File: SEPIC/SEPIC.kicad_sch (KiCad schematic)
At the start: 17 parts, among them J1 Screw Terminal, J2 Barrel Jack, J3 Pin Header, J4 Screw Terminal, Q1 IRF520N, U1 HCPL-3120

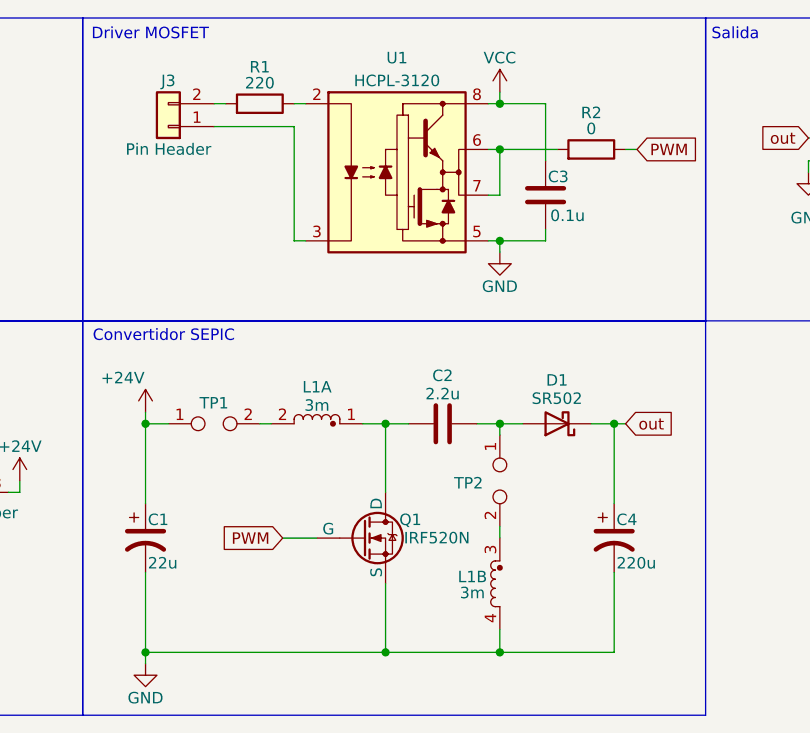
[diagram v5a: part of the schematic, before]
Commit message: Agregar puntos medición corriente
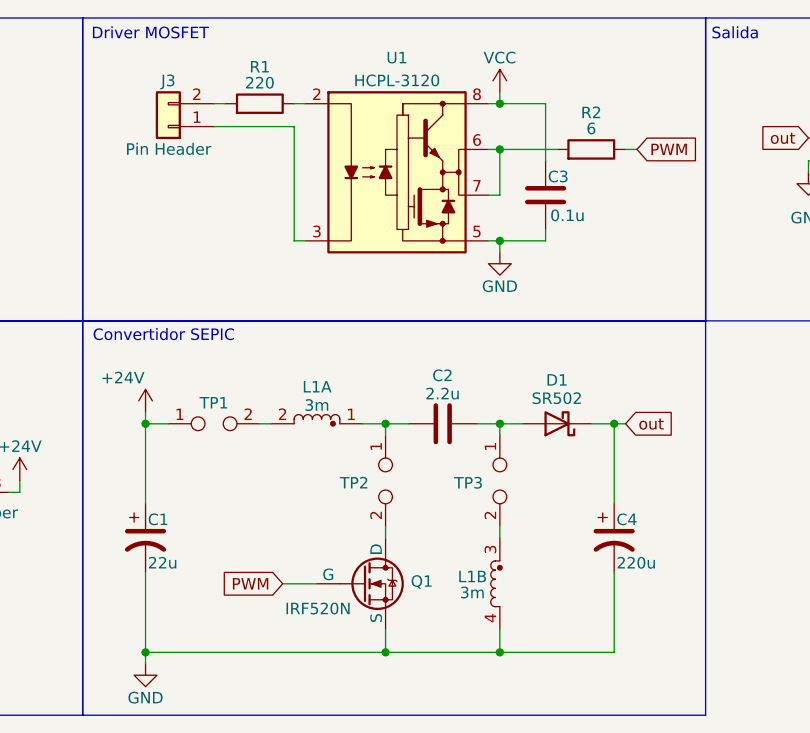
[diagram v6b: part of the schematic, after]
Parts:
- added TP2: Shunt, Resistor_THT:R_Axial_DIN0411_L9.9mm_D3.6mm_P12.70mm_Horizontal, symbol Connector:TestPoint_2Pole
- R2: value 0 -> 6
- TP1: footprint TestPoint:TestPoint_2Pads_Pitch5.08mm_Drill1.3mm -> Resistor_THT:R_Axial_DIN0411_L9.9mm_D3.6mm_P12.70mm_Horizontal
- TP3: renamed from TP2; footprint TestPoint:TestPoint_2Pads_Pitch5.08mm_Drill1.3mm -> Resistor_THT:R_Axial_DIN0411_L9.9mm_D3.6mm_P12.70mm_Horizontal
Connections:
- net at C2.1, L1.1: now also TP2.1; no longer Q1.2 (D)
- new net: Q1.2 (D), TP2.2
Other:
- moved on the sheet: Q1
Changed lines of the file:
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@@
 	(wire
 		(pts
-			(xy 88.9 80.01) (xy 92.71 80.01)
+			(xy 88.9 85.09) (xy 92.71 85.09)
 		)
 		(stroke
@@
 	(wire
 		(pts
-			(xy 100.33 67.31) (xy 100.33 74.93)
-		)
-		(stroke
-			(width 0)
-			(type default)
-		)
-	)
-	(wire
-		(pts
-			(xy 100.33 85.09) (xy 100.33 92.71)
+			(xy 100.33 67.31) (xy 100.33 68.58)
 		)
 		(stroke
@@
 	(wire
 		(pts
+			(xy 100.33 90.17) (xy 100.33 92.71)
+		)
+		(stroke
+			(width 0)
+			(type default)
+		)
+	)
+	(wire
+		(pts
 			(xy 113.03 46.99) (xy 113.03 48.26)
 		)
@@
 		(pts
 			(xy 123.19 67.31) (xy 125.73 67.31)
+		)
+		(stroke
+			(width 0)
+			(type default)
+		)
+	)
+	(wire
+		(pts
+			(xy 100.33 78.74) (xy 100.33 80.01)
 		)
 		(stroke
@@
 	(global_label "PWM"
 		(shape input)
-		(at 88.9 80.01 180)
+		(at 88.9 85.09 180)
 		(fields_autoplaced yes)
 		(effects
@@
 		)
 		(property "Intersheetrefs" "${INTERSHEET_REFS}"
-			(at 81.742 80.01 0)
+			(at 81.742 85.09 0)
 			(effects
 				(font
@@
 		(on_board yes)
 		(dnp no)
-		(property "Reference" "TP2"
+		(property "Reference" "TP3"
 			(at 107.95 73.914 90)
 			(effects
@@
 			)
 		)
-		(property "Footprint" "TestPoint:TestPoint_2Pads_Pitch5.08mm_Drill1.3mm"
+		(property "Footprint" "Resistor_THT:R_Axial_DIN0411_L9.9mm_D3.6mm_P12.70mm_Horizontal"
 			(at 113.03 73.66 0)
 			(effects
@@
 			(project ""
 				(path "/cb0f21c9-e6cc-49b2-a40a-07d77f15ad11"
-					(reference "TP2")
+					(reference "TP3")
 					(unit 1)
 				)
@@
 			)
 		)
-		(property "Value" "0"
+		(property "Value" "6"
 			(at 123.19 34.544 90)
 			(effects
@@
 	)
 	(symbol
+		(lib_id "Connector:TestPoint_2Pole")
+		(at 100.33 73.66 270)
+		(unit 1)
+		(exclude_from_sim no)
+		(in_bom yes)
+		(on_board yes)
+		(dnp no)
+		(property "Reference" "TP2"
+			(at 95.25 73.914 90)
+			(effects
+				(font
+					(size 1.27 1.27)
+				)
+				(justify left)
+			)
+		)
+		(property "Value" "Shunt"
+			(at 99.06 74.93 0)
+			(effects
+				(font
+					(size 1.27 1.27)
+				)
+				(justify left)
+				(hide yes)
+			)
+		)
+		(property "Footprint" "Resistor_THT:R_Axial_DIN0411_L9.9mm_D3.6mm_P12.70mm_Horizontal"
+			(at 100.33 73.66 0)
+			(effects
+				(font
+					(size 1.27 1.27)
+				)
+				(hide yes)
+			)
+		)
+		(property "Datasheet" "~"
+			(at 100.33 73.66 0)
+			(effects
+				(font
+					(size 1.27 1.27)
+				)
+				(hide yes)
+			)
+		)
+		(property "Description" "2-polar test point"
+			(at 100.33 73.66 0)
+			(effects
+				(font
+					(size 1.27 1.27)
+				)
+				(hide yes)
+			)
+		)
+		(pin "2"
+		)
+		(pin "1"
+		)
+		(instances
+			(project "SEPIC"
+				(path "/cb0f21c9-e6cc-49b2-a40a-07d77f15ad11"
+					(reference "TP2")
+					(unit 1)
+				)
+			)
+		)
+	)
+	(symbol
 		(lib_id "power:VCC")
 		(at 113.03 30.48 0)
@@
 			)
 		)
-		(property "Footprint" "TestPoint:TestPoint_2Pads_Pitch5.08mm_Drill1.3mm"
+		(property "Footprint" "Resistor_THT:R_Axial_DIN0411_L9.9mm_D3.6mm_P12.70mm_Horizontal"
 			(at 81.28 67.31 0)
 			(effects
@@
 	(symbol
 		(lib_id "Simulation_SPICE:NMOS")
-		(at 97.79 80.01 0)
+		(at 97.79 85.09 0)
 		(unit 1)
 		(exclude_from_sim no)
@@
 		(dnp no)
 		(property "Reference" "Q1"
-			(at 101.854 77.978 0)
+			(at 103.124 84.836 0)
 			(effects
 				(font
@@
 		)
 		(property "Value" "IRF520N"
-			(at 102.362 80.01 0)
+			(at 89.154 87.884 0)
 			(effects
 				(font
@@
 		)
 		(property "Footprint" "Package_TO_SOT_THT:TO-220-3_Vertical"
-			(at 102.87 77.47 0)
+			(at 102.87 82.55 0)
 			(effects
 				(font
@@
 		)
 		(property "Datasheet" "https://www.infineon.com/assets/row/public/documents/24/49/infineon-irf520n-datasheet-en.pdf"
-			(at 97.79 92.71 0)
+			(at 97.79 97.79 0)
 			(effects
 				(font
@@
 		)
 		(property "Description" "Transistor MOSFET canal N"
-			(at 97.79 80.01 0)
+			(at 97.79 85.09 0)
 			(effects
 				(font
@@
 		)
 		(property "Sim.Device" "NMOS"
-			(at 97.79 97.155 0)
+			(at 97.79 102.235 0)
 			(effects
 				(font
@@
 		)
 		(property "Sim.Type" "VDMOS"
-			(at 97.79 99.06 0)
+			(at 97.79 104.14 0)
 			(effects
 				(font
@@
 		)
 		(property "Sim.Pins" "1=D 2=G 3=S"
-			(at 97.79 95.25 0)
-			(effects
-				(font
+			(at 97.79 100.33 0)
+			(effects
+				(font

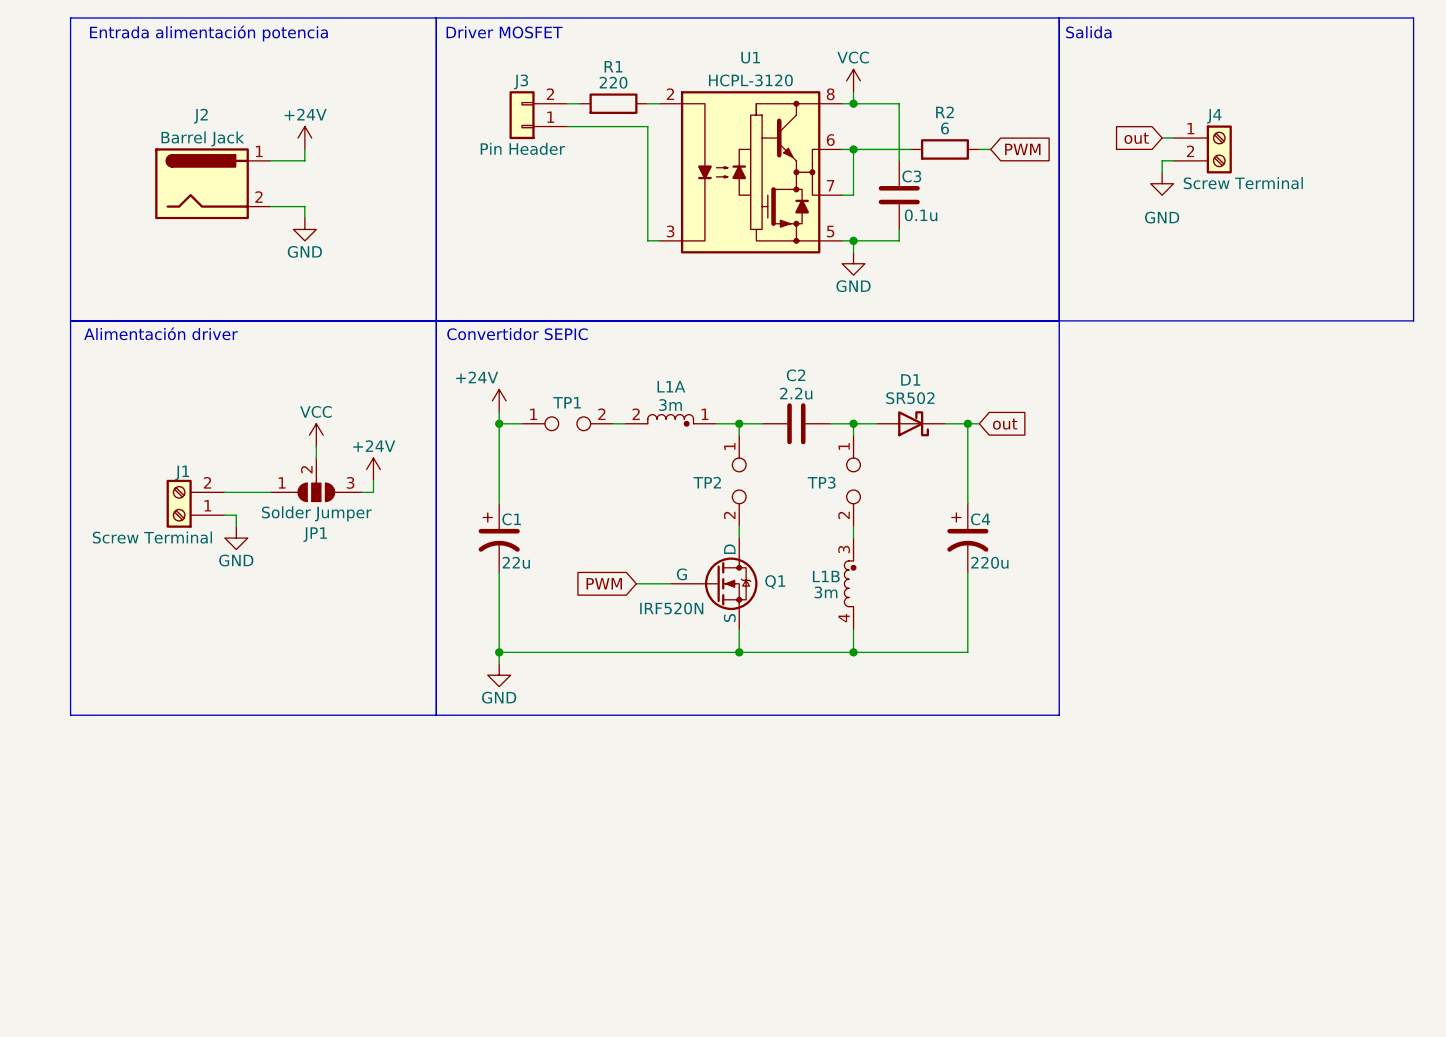
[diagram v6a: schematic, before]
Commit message: Condensadores salida
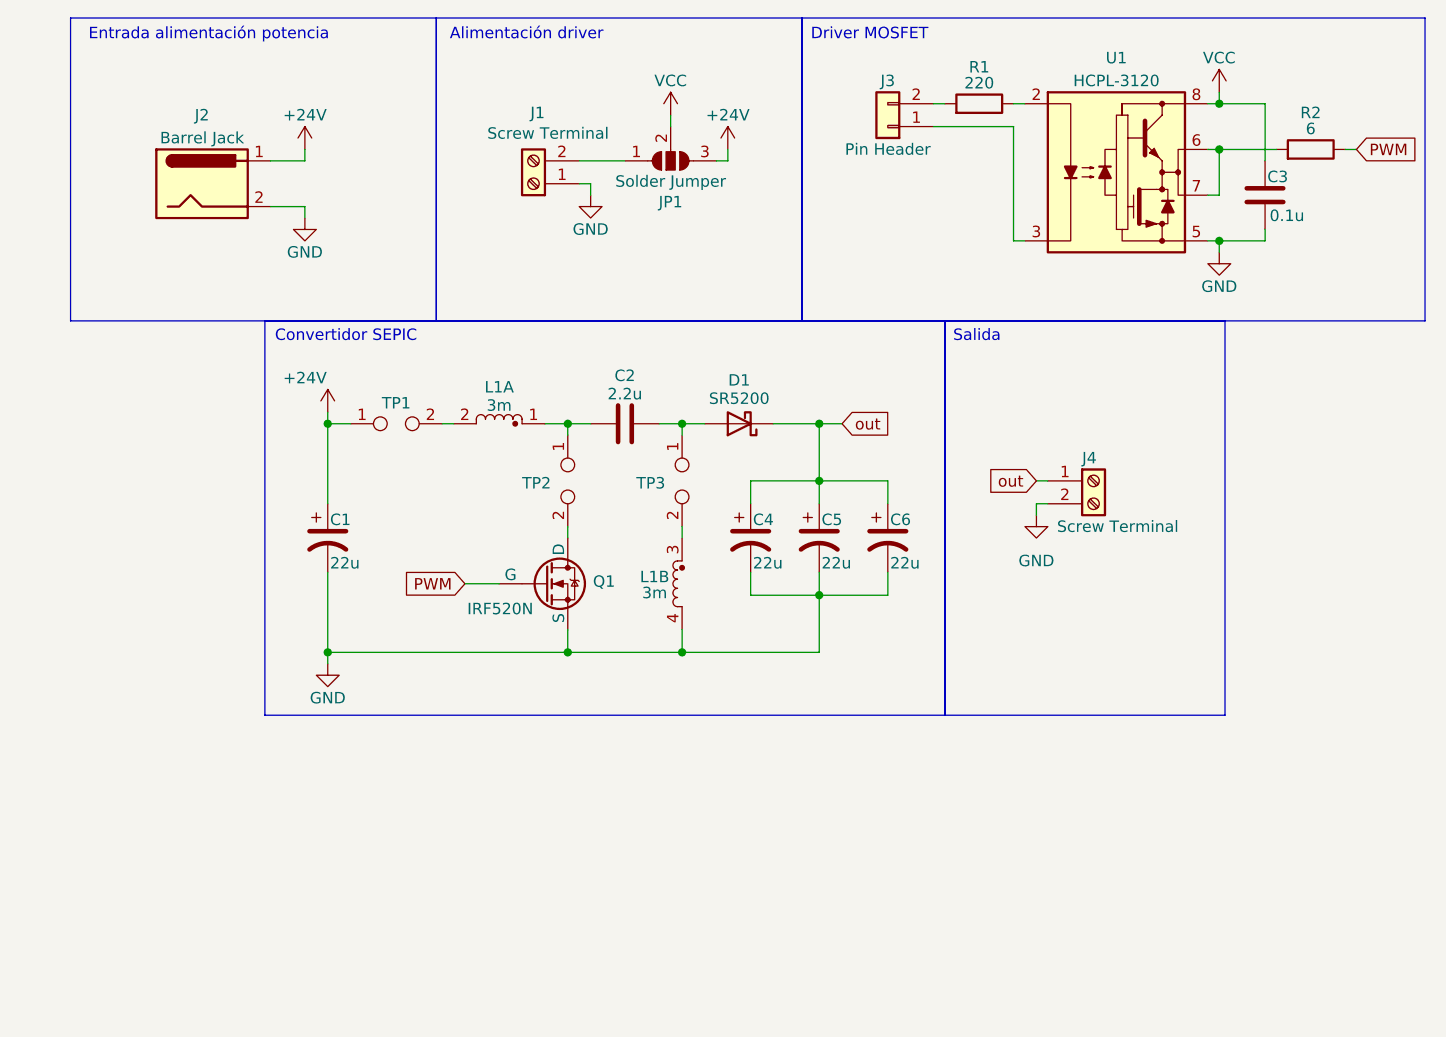
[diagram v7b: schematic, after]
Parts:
- added C5, C6: 22u, Capacitor_THT:C_Radial_D8.0mm_H11.5mm_P3.50mm, symbol Device:C_Polarized_US
- C4: value 220u -> 22u; footprint Capacitor_THT:C_Radial_D16.0mm_H25.0mm_P7.50mm -> Capacitor_THT:C_Radial_D8.0mm_H11.5mm_P3.50mm
- D1: value SR502 -> SR5200
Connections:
- net GND: now also C5.2, C6.2
- net out: now also C5.1, C6.1
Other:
- moved on the sheet: C1, C2, C3, C4, D1, J1, J3, J4, JP1, L1A, L1B, Q1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

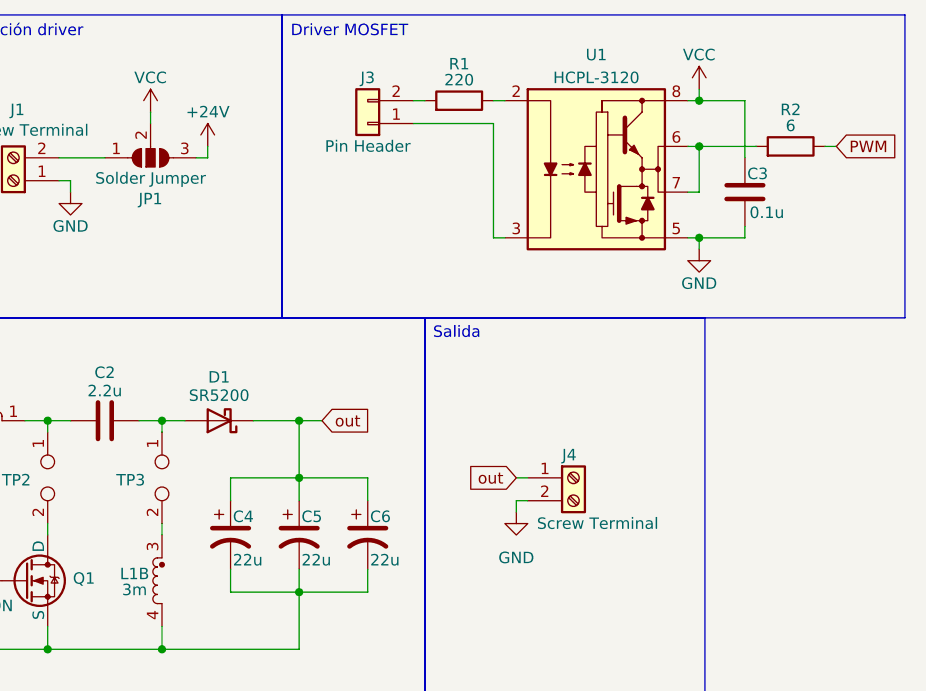
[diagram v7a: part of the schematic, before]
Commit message: Simulacion con valores medidos
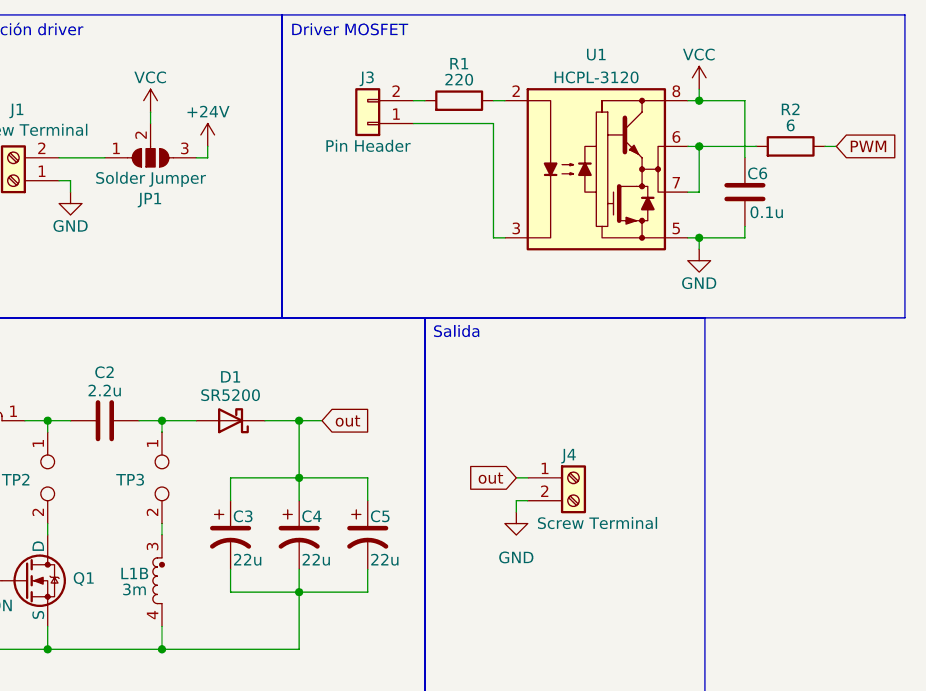
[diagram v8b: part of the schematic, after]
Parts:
- renumbered C4 to C3, C5 to C4, C6 to C5, C3 to C6
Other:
- moved on the sheet: D1
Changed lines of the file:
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@@
+	)
+	(junction
+		(at 109.22 67.31)
+		(diameter 0)
+		(color 0 0 0 0)
 	)
 	(junction
@@
 	)
 	(junction
-		(at 109.22 67.31)
-		(diameter 0)
-		(color 0 0 0 0)
-	)
-	(junction
 		(at 109.22 86.36)
 		(diameter 0)
@@
 	(wire
 		(pts
-			(xy 93.98 67.31) (xy 96.52 67.31)
+			(xy 93.98 67.31) (xy 97.79 67.31)
 		)
 		(stroke
@@
 	(wire
 		(pts
+			(xy 105.41 67.31) (xy 109.22 67.31)
+		)
+		(stroke
+			(width 0)
+			(type default)
+		)
+	)
+	(wire
+		(pts
 			(xy 109.22 67.31) (xy 111.76 67.31)
 		)
@@
 		(pts
 			(xy 91.44 67.31) (xy 93.98 67.31)
-		)
-		(stroke
-			(width 0)
-			(type default)
-		)
-	)
-	(wire
-		(pts
-			(xy 104.14 67.31) (xy 109.22 67.31)
 		)
 		(stroke
@@
 		(on_board yes)
 		(dnp no)
-		(property "Reference" "C3"
+		(property "Reference" "C6"
 			(at 159.004 39.878 0)
 			(effects
@@
 			(project ""
 				(path "/cb0f21c9-e6cc-49b2-a40a-07d77f15ad11"
-					(reference "C3")
+					(reference "C6")
 					(unit 1)
 				)
@@
 	(symbol
 		(lib_id "Device:D_Schottky")
-		(at 100.33 67.31 180)
+		(at 101.6 67.31 180)
 		(unit 1)
 		(exclude_from_sim no)
@@
 		(dnp no)
 		(property "Reference" "D1"
-			(at 100.33 62.484 0)
+			(at 101.6 62.484 0)
 			(effects
 				(font
@@
 		)
 		(property "Value" "SR5200"
-			(at 100.33 64.516 0)
+			(at 101.6 64.516 0)
 			(effects
 				(font
@@
 		)
 		(property "Footprint" "Diode_THT:D_A-405_P7.62mm_Horizontal"
-			(at 100.33 67.31 0)
+			(at 101.6 67.31 0)
 			(effects
 				(font
@@
 		)
 		(property "Datasheet" "https://mm.digikey.com/Volume0/opasdata/d220001/medias/docus/827/SR502-506.pdf"
-			(at 100.33 67.31 0)
+			(at 101.6 67.31 0)
 			(effects
 				(font
@@
 		)
 		(property "Description" "Diodo Schottky"
-			(at 100.33 67.31 0)
+			(at 101.6 67.31 0)
 			(effects
 				(font
@@
 		)
 		(property "Sim.Device" "D"
-			(at 100.33 67.31 0)
+			(at 101.6 67.31 0)
 			(effects
 				(font
@@
 		)
 		(property "Sim.Pins" "1=A 2=K"
-			(at 100.33 67.31 0)
+			(at 101.6 67.31 0)
 			(effects
 				(font
@@
 		(on_board yes)
 		(dnp no)
-		(property "Reference" "C4"
+		(property "Reference" "C3"
 			(at 101.854 77.978 0)
 			(effects
@@
 			(project ""
 				(path "/cb0f21c9-e6cc-49b2-a40a-07d77f15ad11"
-					(reference "C4")
+					(reference "C3")
 					(unit 1)
 				)
@@
 		(on_board yes)
 		(dnp no)
-		(property "Reference" "C5"
+		(property "Reference" "C4"
 			(at 109.474 77.978 0)
 			(effects
@@
 			(project "SEPIC"
 				(path "/cb0f21c9-e6cc-49b2-a40a-07d77f15ad11"
-					(reference "C5")
+					(reference "C4")
 					(unit 1)
 				)
@@
 		(on_board yes)
 		(dnp no)
-		(property "Reference" "C6"
+		(property "Reference" "C5"
 			(at 117.094 77.978 0)
 			(effects
@@
 			(project "SEPIC"
 				(path "/cb0f21c9-e6cc-49b2-a40a-07d77f15ad11"
-					(reference "C6")
+					(reference "C5")
 					(unit 1)
 				)
